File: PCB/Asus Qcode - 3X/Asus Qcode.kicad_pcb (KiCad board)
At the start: 2 copper layers, 121.9 x 49.5 mm, 22 parts, among them J1 COM_DEBUG, J2 Conn_01x03_Pin, J3 Conn_01x02_Pin, SW1 Recall Codes

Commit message: Fix PCB routing issues
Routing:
- net /dp: track 159.6 -> 171.1 mm
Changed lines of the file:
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@@
   (via (at 102.87 48.26) (size 1.6) (drill 0.8) (layers "F.Cu" "B.Cu") (net 5))
   (via (at 132.08 48.26) (size 1.6) (drill 0.8) (layers "F.Cu" "B.Cu") (net 5))
+  (segment (start 73.66 48.26) (end 90.17 48.26) (width 0.6) (layer "B.Cu") (net 5))
   (segment (start 132.08 48.26) (end 132.08 36.7075) (width 0.6) (layer "B.Cu") (net 5))
+  (segment (start 90.17 48.26) (end 102.87 48.26) (width 0.6) (layer "B.Cu") (net 5))
   (segment (start 38.735 36.83) (end 50.165 48.26) (width 0.6) (layer "B.Cu") (net 5))
   (segment (start 60.4475 48.1375) (end 60.4475 36.83) (width 0.6) (layer "B.Cu") (net 5))
+  (segment (start 90.17 36.7075) (end 90.17 48.26) (width 0.6) (layer "B.Cu") (net 5))
   (segment (start 73.66 48.26) (end 73.66 36.7075) (width 0.6) (layer "B.Cu") (net 5))
   (segment (start 50.165 48.26) (end 60.325 48.26) (width 0.6) (layer "B.Cu") (net 5))
-  (segment (start 73.66 48.26) (end 102.87 48.26) (width 0.6) (layer "B.Cu") (net 5))
   (segment (start 60.325 48.26) (end 60.4475 48.1375) (width 0.6) (layer "B.Cu") (net 5))
   (segment (start 119.38 48.26) (end 119.38 36.7075) (width 0.6) (layer "B.Cu") (net 5))

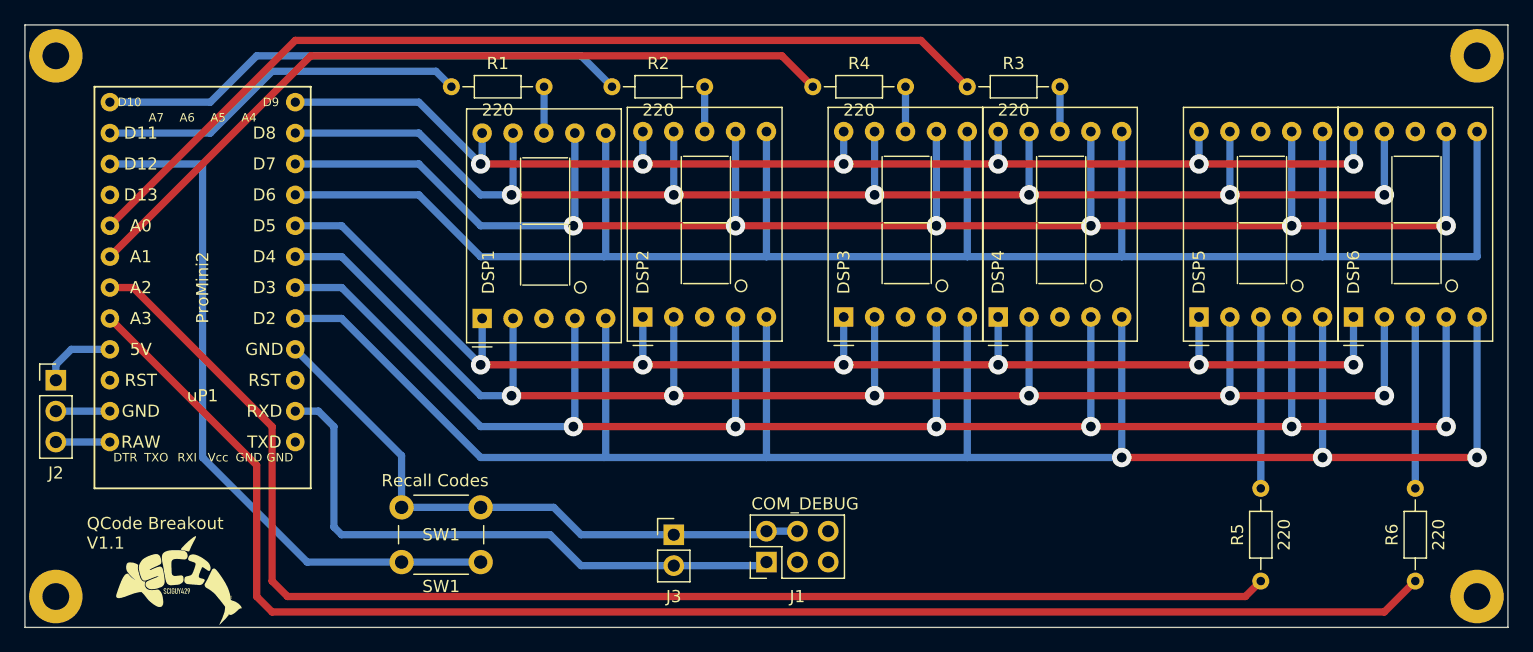
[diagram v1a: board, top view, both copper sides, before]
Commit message: More PCB fixes
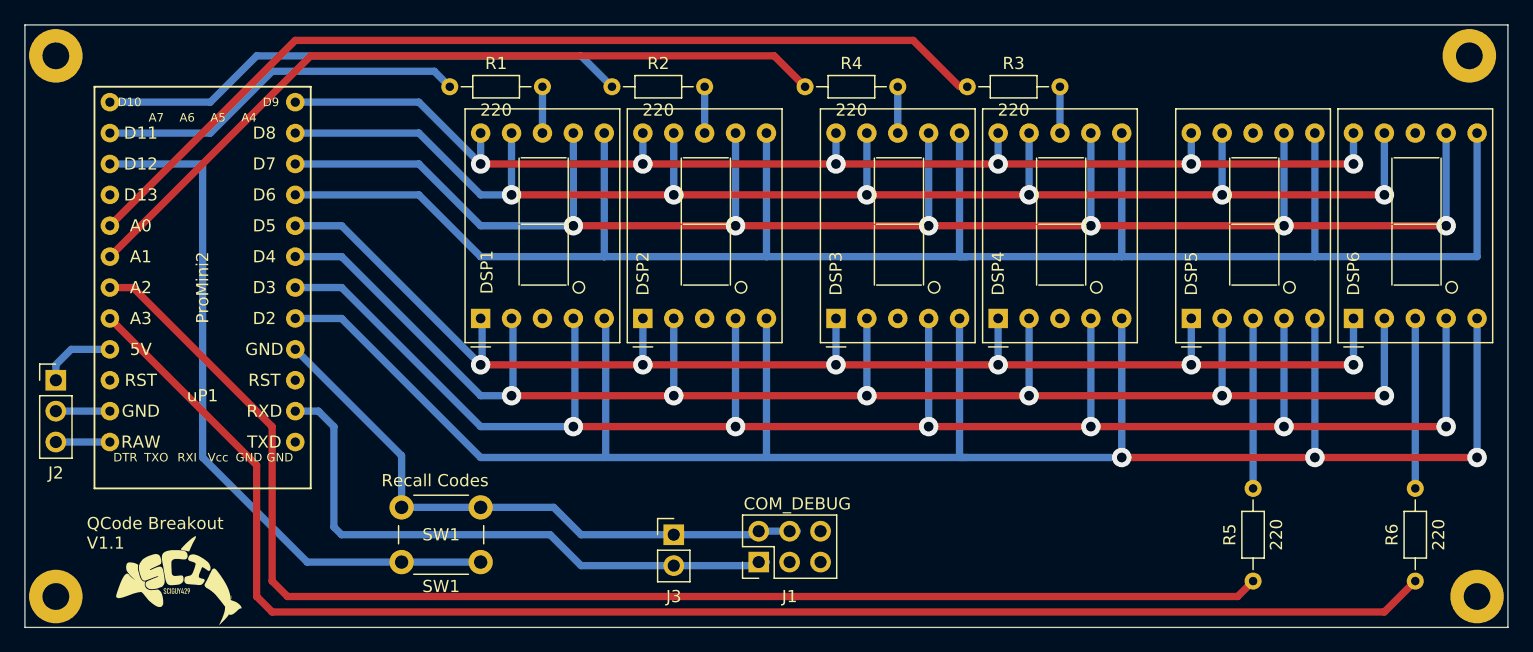
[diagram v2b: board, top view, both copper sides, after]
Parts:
- moved DSP3 0.65 mm to (79.4, 36.8)
- moved DSP5 0.65 mm to (108.6, 36.8)
- moved REF** 0.64 mm to (131.4, 15.2)
- moved R4 0.64 mm to (76.8, 17.8)
- moved J1 0.63 mm to (73.0, 56.9)
- moved R5 0.63 mm to (113.7, 58.4)
- moved R1 0.13 mm to (47.6, 17.8)
- moved DSP1 0.12 mm to (50.2, 36.8)
- moved DSP2 0.12 mm to (63.5, 36.8)
- moved DSP4 0.12 mm to (92.7, 36.8)
- moved DSP6 0.12 mm to (121.9, 36.8)
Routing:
- net Net-(uP1-PC0/A0): track 78.4 -> 77.7 mm
- net Net-(uP1-PC2/A2): track 113.1 -> 112.5 mm
- net Net-(uP1-PC1/A1): track 65.7 -> 65.0 mm
- net /g: track 105.0 -> 105.5 mm
- net /f: track 122.8 -> 123.3 mm
- net /b: track 160.9 -> 161.4 mm
- net /a: track 143.1 -> 143.6 mm
